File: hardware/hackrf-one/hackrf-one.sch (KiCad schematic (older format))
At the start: 0 parts

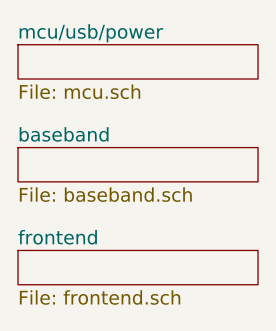
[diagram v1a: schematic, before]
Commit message: Improved Bias T design to use two inductors
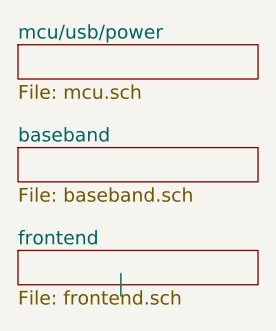
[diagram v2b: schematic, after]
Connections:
- wire segments 0 -> 1
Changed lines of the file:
@@
 F1 "mcu.sch" 60
 $EndSheet
+Wire Wire Line
+	3000 3400 3000 3500
 $EndSCHEMATC

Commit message: Updated U1, 2, 5, 6, 10, 11 from SKY13350 to SKY13453
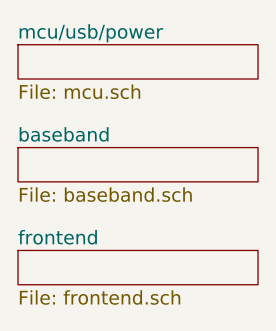
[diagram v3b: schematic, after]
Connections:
- wire segments 1 -> 0
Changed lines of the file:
@@
 F1 "mcu.sch" 60
 $EndSheet
-Wire Wire Line
-	3000 3400 3000 3500
 $EndSCHEMATC

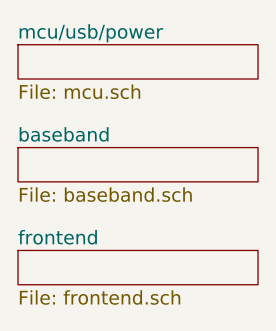
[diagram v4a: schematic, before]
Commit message: Documented the production procedure for manufacturing files
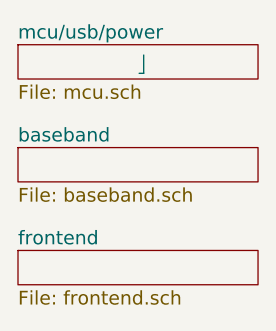
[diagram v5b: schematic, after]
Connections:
- wire segments 0 -> 2
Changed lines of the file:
@@
 F1 "mcu.sch" 60
 $EndSheet
+Wire Wire Line
+	3080 2525 3100 2525
+Wire Wire Line
+	3100 2525 3100 2445
 $EndSCHEMATC
